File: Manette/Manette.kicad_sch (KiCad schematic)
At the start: 19 parts, among them J2 Barrel_Jack, SW1 SW_SPST, SW2 SW_Push, SW3 SW_Push, SW4 SW_Push, SW5 SW_Push, SW6 SW_Push, U1 LD1117S33TR_SOT223, U2 ESP32-S3-WROOM-1

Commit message: feat(manette): add the pcb design for the game controller
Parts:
- C1, C2, C3: footprint (none) -> Capacitor_SMD:C_1206_3216Metric
- J2: footprint (none) -> Connector_BarrelJack:BarrelJack_Wuerth_6941xx301002
- R1, R2, R3, R4, R5, R6: footprint (none) -> Resistor_SMD:R_1206_3216Metric
- SW1: footprint (none) -> Button_Switch_THT:SW_Slide_SPDT_Straight_CK_OS102011MS2Q
- SW2, SW3, SW4, SW5, SW6: footprint (none) -> Button_Switch_THT:SW_Tactile_Straight_KSA0Axx1LFTR
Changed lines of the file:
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@@
 			)
 		)
-		(property "Footprint" ""
+		(property "Footprint" "Connector_BarrelJack:BarrelJack_Wuerth_6941xx301002"
 			(at 102.87 25.146 0)
 			(effects
@@
 			)
 		)
-		(property "Footprint" ""
+		(property "Footprint" "Capacitor_SMD:C_1206_3216Metric"
 			(at 86.6648 101.6 0)
 			(effects
@@
 			)
 		)
-		(property "Footprint" ""
+		(property "Footprint" "Button_Switch_THT:SW_Tactile_Straight_KSA0Axx1LFTR"
 			(at 250.19 60.96 0)
 			(effects
@@
 			)
 		)
-		(property "Footprint" ""
+		(property "Footprint" "Capacitor_SMD:C_1206_3216Metric"
 			(at 143.51 42.8752 0)
 			(effects
@@
 			)
 		)
-		(property "Footprint" ""
+		(property "Footprint" "Button_Switch_THT:SW_Tactile_Straight_KSA0Axx1LFTR"
 			(at 251.46 96.52 0)
 			(effects
@@
 			)
 		)
-		(property "Footprint" ""
+		(property "Footprint" "Capacitor_SMD:C_1206_3216Metric"
 			(at 177.8 44.1452 0)
 			(effects
@@
 			)
 		)
-		(property "Footprint" ""
+		(property "Footprint" "Resistor_SMD:R_1206_3216Metric"
 			(at 135.382 62.23 90)
 			(effects
@@
 			)
 		)
-		(property "Footprint" ""
+		(property "Footprint" "Button_Switch_THT:SW_Tactile_Straight_KSA0Axx1LFTR"
 			(at 215.9 60.96 0)
 			(effects
@@
 			)
 		)
-		(property "Footprint" ""
+		(property "Footprint" "Resistor_SMD:R_1206_3216Metric"
 			(at 248.412 50.8 90)
 			(effects
@@
 			)
 		)
-		(property "Footprint" ""
+		(property "Footprint" "Resistor_SMD:R_1206_3216Metric"
 			(at 249.682 85.09 90)
 			(effects
@@
 			)
 		)
-		(property "Footprint" ""
+		(property "Footprint" "Resistor_SMD:R_1206_3216Metric"
 			(at 214.122 121.92 90)
 			(effects
@@
 			)
 		)
-		(property "Footprint" ""
+		(property "Footprint" "Button_Switch_THT:SW_Tactile_Straight_KSA0Axx1LFTR"
 			(at 215.9 96.52 0)
 			(effects
@@
 			)
 		)
-		(property "Footprint" ""
+		(property "Footprint" "Button_Switch_THT:SW_Tactile_Straight_KSA0Axx1LFTR"
 			(at 215.9 134.62 0)
 			(effects
@@
 			)
 		)
-		(property "Footprint" ""
+		(property "Footprint" "Resistor_SMD:R_1206_3216Metric"
 			(at 214.122 50.8 90)
 			(effects
@@
 			)
 		)
-		(property "Footprint" ""
+		(property "Footprint" "Button_Switch_THT:SW_Slide_SPDT_Straight_CK_OS102011MS2Q"
 			(at 135.89 27.94 0)
 			(effects
@@
 			)
 		)
-		(property "Footprint" ""
+		(property "Footprint" "Resistor_SMD:R_1206_3216Metric"
 			(at 214.122 85.09 90)
 			(effects

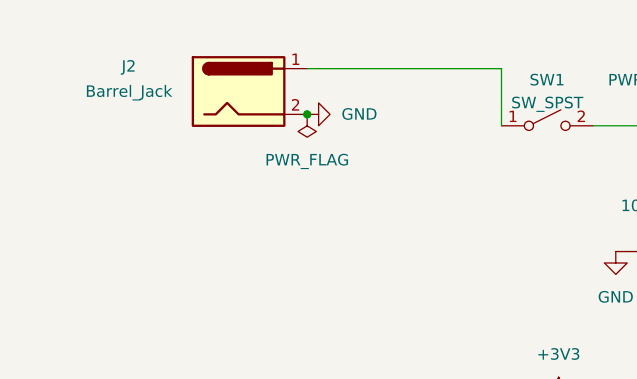
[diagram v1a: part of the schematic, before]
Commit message: fix(manette): removed the barrel jack with a 2 pin connector to place the 4 battery holder
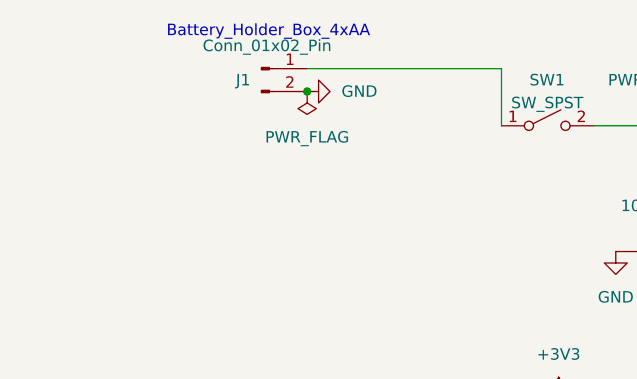
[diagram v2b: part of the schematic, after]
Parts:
- removed J2: Barrel_Jack, Connector_BarrelJack:BarrelJack_Wuerth_6941xx301002, symbol Connector:Barrel_Jack
- added J1: Conn_01x02_Pin, Connector_PinHeader_2.54mm:PinHeader_1x02_P2.54mm_Vertical, symbol Connector:Conn_01x02_Pin
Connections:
- net GND: now also J1.2 (Pin_2)
- net at SW1.1 (A): now also J1.1 (Pin_1)
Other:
- note added: "Battery_Holder_Box_4xAA"
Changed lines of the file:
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@@
 		(company "EPITA")
+	)
+	(text "Battery_Holder_Box_4xAA"
+		(exclude_from_sim no)
+		(at 104.902 17.526 0)
+		(effects
+			(font
+				(size 1.27 1.27)
+			)
+		)
+	)
+	(junction
+		(at 109.22 24.13)
+		(diameter 0)
+		(color 0 0 0 0)
 	)
 	(junction
@@
 	(junction
 		(at 156.21 27.94)
-		(diameter 0)
-		(color 0 0 0 0)
-	)
-	(junction
-		(at 109.22 26.67)
 		(diameter 0)
 		(color 0 0 0 0)
@@
 	)
 	(symbol
-		(lib_id "Connector:Barrel_Jack")
-		(at 101.6 24.13 0)
-		(unit 1)
-		(exclude_from_sim no)
-		(in_bom yes)
-		(on_board yes)
-		(dnp no)
-		(property "Reference" "J2"
-			(at 89.408 21.336 0)
-			(effects
-				(font
-					(size 1.27 1.27)
-				)
-			)
-		)
-		(property "Value" "Barrel_Jack"
-			(at 89.408 24.13 0)
-			(effects
-				(font
-					(size 1.27 1.27)
-				)
-			)
-		)
-		(property "Footprint" "Connector_BarrelJack:BarrelJack_Wuerth_6941xx301002"
-			(at 102.87 25.146 0)
-			(effects
-				(font
-					(size 1.27 1.27)
-				)
-				(hide yes)
-			)
-		)
-		(property "Datasheet" "~"
-			(at 102.87 25.146 0)
-			(effects
-				(font
-					(size 1.27 1.27)
-				)
-				(hide yes)
-			)
-		)
-		(property "Description" "DC Barrel Jack"
-			(at 101.6 24.13 0)
-			(effects
-				(font
-					(size 1.27 1.27)
-				)
-				(hide yes)
-			)
-		)
-		(pin "2"
-		)
-		(pin "1"
-		)
-		(instances
-			(project ""
-				(path "/7311fa03-01b7-4883-ab42-55d7db8f2f4b"
-					(reference "J2")
-					(unit 1)
-				)
-			)
-		)
-	)
-	(symbol
 		(lib_id "Device:C_Polarized")
 		(at 87.63 97.79 0)
@@
 	)
 	(symbol
+		(lib_id "Connector:Conn_01x02_Pin")
+		(at 104.14 21.59 0)
+		(unit 1)
+		(exclude_from_sim no)
+		(in_bom yes)
+		(on_board yes)
+		(dnp no)
+		(property "Reference" "J1"
+			(at 102.108 22.86 0)
+			(effects
+				(font
+					(size 1.27 1.27)
+				)
+			)
+		)
+		(property "Value" "Conn_01x02_Pin"
+			(at 104.775 19.05 0)
+			(effects
+				(font
+					(size 1.27 1.27)
+				)
+			)
+		)
+		(property "Footprint" "Connector_PinHeader_2.54mm:PinHeader_1x02_P2.54mm_Vertical"
+			(at 104.14 21.59 0)
+			(effects
+				(font
+					(size 1.27 1.27)
+				)
+				(hide yes)
+			)
+		)
+		(property "Datasheet" "~"
+			(at 104.14 21.59 0)
+			(effects
+				(font
+					(size 1.27 1.27)
+				)
+				(hide yes)
+			)
+		)
+		(property "Description" "Generic connector, single row, 01x02, script generated"
+			(at 104.14 21.59 0)
+			(effects
+				(font
+					(size 1.27 1.27)
+				)
+				(hide yes)
+			)
+		)
+		(pin "1"
+		)
+		(pin "2"
+		)
+		(instances
+			(project ""
+				(path "/7311fa03-01b7-4883-ab42-55d7db8f2f4b"
+					(reference "J1")
+					(unit 1)
+				)
+			)
+		)
+	)
+	(symbol
 		(lib_id "power:PWR_FLAG")
-		(at 109.22 26.67 0)
+		(at 109.22 24.13 0)
 		(mirror x)
 		(unit 1)
@@
 		(dnp no)
 		(property "Reference" "#FLG01"
-			(at 109.22 28.575 0)
+			(at 109.22 26.035 0)
 			(effects
 				(font
@@
 		)
 		(property "Value" "PWR_FLAG"
-			(at 109.22 31.75 0)
+			(at 109.22 29.21 0)
 			(effects
 				(font
@@
 		)
 		(property "Footprint" ""
-			(at 109.22 26.67 0)
+			(at 109.22 24.13 0)
 			(effects
 				(font
@@
 		)
 		(property "Datasheet" "~"
-			(at 109.22 26.67 0)
+			(at 109.22 24.13 0)
 			(effects
 				(font
@@
 		)
 		(property "Description" "Special symbol for telling ERC where power comes from"
-			(at 109.22 26.67 0)
+			(at 109.22 24.13 0)
 			(effects
 				(font
@@
 	(symbol
 		(lib_id "power:GND")
-		(at 109.22 26.67 90)
+		(at 109.22 24.13 90)
 		(unit 1)
 		(exclude_from_sim no)
@@
 		(fields_autoplaced yes)
 		(property "Reference" "#PWR03"
-			(at 115.57 26.67 0)
+			(at 115.57 24.13 0)
 			(effects
 				(font
@@
 		)
 		(property "Value" "GND"
-			(at 113.03 26.6699 90)
+			(at 113.03 24.1299 90)
 			(effects
 				(font
@@
 		)
 		(property "Footprint" ""
-			(at 109.22 26.67 0)
+			(at 109.22 24.13 0)
 			(effects
 				(font
@@
 		)
 		(property "Datasheet" ""
-			(at 109.22 26.67 0)
+			(at 109.22 24.13 0)
 			(effects
 				(font
@@
 		)
 		(property "Description" "Power symbol creates a global label with name \"GND\" , ground"
-			(at 109.22 26.67 0)
-			(effects
-				(font
+			(at 109.22 24.13 0)
+			(effects
+				(font
